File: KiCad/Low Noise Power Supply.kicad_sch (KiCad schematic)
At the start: 27 parts, among them Q401 FMMT614TA, Q402 FMMT734, U401 L78L15_SOT89, U402 PESE1-S5-S24-M, U403 L78L05, U404 L79L15_SOT89

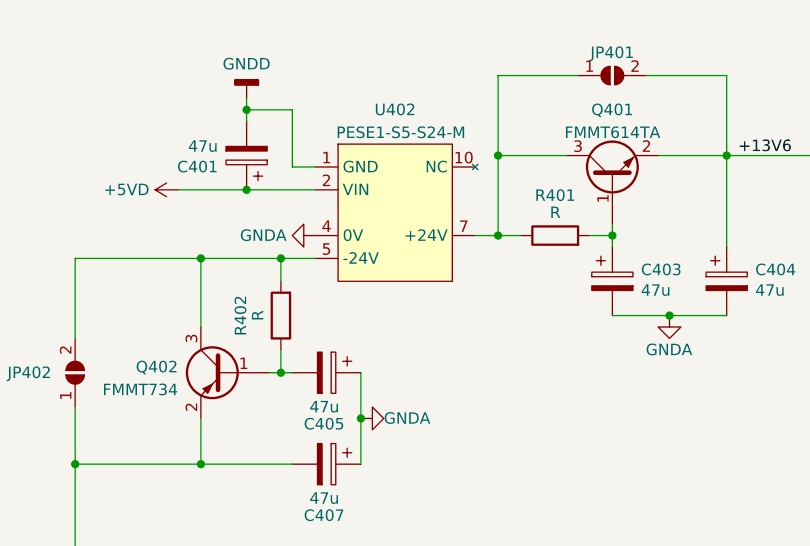
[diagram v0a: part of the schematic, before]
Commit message: Updated some designators and added component list
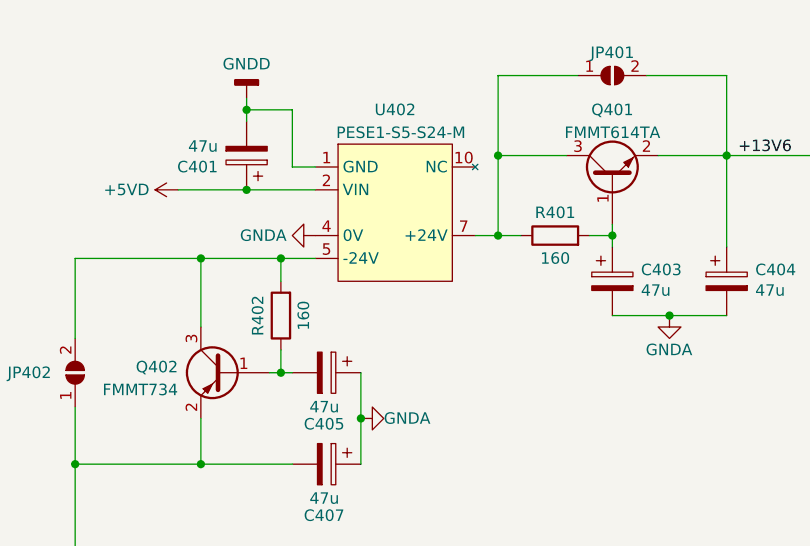
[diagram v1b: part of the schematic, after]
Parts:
- R401, R402: value R -> 160
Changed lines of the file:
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@@
   (symbol (lib_id "Device:R") (at 139.7 68.58 90) (unit 1)
     (in_bom yes) (on_board yes) (dnp no)
-    (property "Reference" "R401" (at 139.7 64.135 90)
-      (effects (font (size 1.27 1.27)))
-    )
-    (property "Value" "R" (at 139.7 66.04 90)
+    (property "Reference" "R401" (at 139.7 66.04 90)
+      (effects (font (size 1.27 1.27)))
+    )
+    (property "Value" "160" (at 139.7 71.12 90)
       (effects (font (size 1.27 1.27)))
     )
@@
   (symbol (lib_id "Device:R") (at 109.22 77.47 180) (unit 1)
     (in_bom yes) (on_board yes) (dnp no)
-    (property "Reference" "R402" (at 104.775 77.47 90)
-      (effects (font (size 1.27 1.27)))
-    )
-    (property "Value" "R" (at 106.68 77.47 90)
-      (effects (font (size 1.27 1.27)))
-    )
+    (property "Reference" "R402" (at 106.68 77.47 90)
+      (effects (font (size 1.27 1.27)))
+    )
+    (property "Value" "160" (at 111.76 77.47 90)
+      (effects (font (size 1.27 1.27)))
+    )

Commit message: Cleaned up a few things
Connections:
- net +13V6: no longer names the net of C404.1, D401.1 (K), JP401.2 (B), Q401.2 (E), U401.3 (IN)
- net -13V6: no longer names the net of C407.2, D405.2 (A), JP402.1 (A), Q402.2 (E), U404.2 (VI)
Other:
- note added: "+15V REGULATOR"
- note added: "+5V REGULATOR"
- note added: "-15V REGULATOR"
- note added: "CAPACITANCE MULTIPLIER"
- note added: "DC-DC CONVERTER"
- company: (none) -> M Morano
- moved on the sheet: C401, C402, C403, C404, C405, C406, C407, C408, D401, D402, D403, D404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
